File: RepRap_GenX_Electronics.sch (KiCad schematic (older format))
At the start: 105 parts, among them J1 AXIS_X, J10 END_Y, J11 END_Z, J12 END_E0, J13 END_E1, J14 HEAT_E1, J15 TEMP_BED, J16 TEMP_E0, J17 TEMP_E1, J18 E1, J19 Conn_ARM_JTAG_SWD_10, J2 AXIS_Y, J20 12V_0, J21 12V_1, J22 FAN_0, J23 FAN_1, J3 MOT_PWR, J3_1 AXIS_Z1, J3_2 AXIS_Z2, J4 E0, J5 HEAT_PWR, J6 HEAT_E0, J7 HEAT_BED, J8 USB_B_Micro, J9 END_X, Q1 IRLIZ44N, Q2 IRLIZ44N, Q3 IRLIZ44N, Q4 DMN2300U, Q5 DMN2300U, SW1 SW_Push, U1 STM32F412RGTx, U2 ADP2303ARDZ-5.0, U3 USBLC6-2SC6, U4 TPS62160DSG

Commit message: Added ZVD and 5V breakout for external supply
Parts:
- added J24: Conn_02x02_Counter_Clockwise, Connector_PinHeader_2.54mm:PinHeader_2x02_P2.54mm_Vertical, symbol Connector_Generic:Conn_02x02_Counter_Clockwise
- added Q6: DMMT5401-7(A), Package_SO:SC-74-6_1.5x2.9mm_P0.95mm, symbol Device:Q_DUAL_PNP_PNP_C1B1B2C2E2E1
- added Q7: DMG2305UX, Package_TO_SOT_SMD:SOT-23, symbol Transistor_FET:DMG2301L
- added R19, R4: 10K, Resistor_SMD:R_0603_1608Metric, symbol Device:R
- JP1: footprint Jumper:SolderJumper-2_P1.3mm_Open_TrianglePad1.0x1.5mm -> Connector_PinHeader_2.54mm:PinHeader_1x02_P2.54mm_Vertical
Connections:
- net +5V: now also Q6.6 (E1), Q7.3 (D); no longer C17.2, C5.1, J8.1 (VBUS), U3.5 (VBUS), U4.2 (VIN), U4.3 (EN)
- net GND: now also C13.1, J24.1 (Pin_1), J24.2 (Pin_2), R19.2, R4.2; no longer C13.2
- net at U1.30 (VCAP_1): now also C13.2; no longer C13.1
- new net: Q6.4 (C2), Q7.1 (G), R19.1
- new net: Q6.1 (C1), Q6.2 (B1), Q6.3 (B2), R4.1
- new net ZVD_5V: C17.2, C5.1, J24.3 (Pin_3), J24.4 (Pin_4), J8.1 (VBUS), Q6.5 (E2), Q7.2 (S), U3.5 (VBUS), U4.2 (VIN), U4.3 (EN)
- no-connect marks 13 -> 12
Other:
- note added: ""Ideal" Zero Volt Diode (ZVD)"
- moved on the sheet: C13, J19, J20, J21, XO1

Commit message: Added totem pole drivers for MOSFETs and split main schematic
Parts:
- removed A1, A2, A3, A4, A5: SilentStepStick_SPI, Module:Pololu_Breakout-16_15.2x20.3mm, symbol StepStick:SilentStepStick_SPI
- removed C19, C20, C21, C22, C23, C24, C25, C26, C27, C28: 100nF, Capacitor_SMD:C_0402_1005Metric, symbol Device:C
- removed D2, D3, D4: LED, LED_SMD:LED_0603_1608Metric, symbol Device:LED
- removed D5, D6, D7, D8, D9: D, Diode_SMD:D_SMA, symbol Device:D
- removed J1: AXIS_X, Connector_Molex:Molex_KK-254_AE-6410-04A_1x04_P2.54mm_Vertical, symbol Connector_Generic:Conn_01x04
- removed J10: END_Y, Connector_Molex:Molex_KK-254_AE-6410-03A_1x03_P2.54mm_Vertical, symbol Connector_Generic:Conn_01x03
- removed J11: END_Z, Connector_Molex:Molex_KK-254_AE-6410-03A_1x03_P2.54mm_Vertical, symbol Connector_Generic:Conn_01x03
- removed J12: END_E0, Connector_Molex:Molex_KK-254_AE-6410-03A_1x03_P2.54mm_Vertical, symbol Connector_Generic:Conn_01x03
- removed J13: END_E1, Connector_Molex:Molex_KK-254_AE-6410-03A_1x03_P2.54mm_Vertical, symbol Connector_Generic:Conn_01x03
- removed J14: HEAT_E1, Connector_Molex:Molex_KK-396_A-41791-0002_1x02_P3.96mm_Vertical, symbol Connector_Generic:Conn_01x02
- removed J15: TEMP_BED, Connector_Molex:Molex_KK-254_AE-6410-02A_1x02_P2.54mm_Vertical, symbol Connector_Generic:Conn_01x02
- removed J16: TEMP_E0, Connector_Molex:Molex_KK-254_AE-6410-02A_1x02_P2.54mm_Vertical, symbol Connector_Generic:Conn_01x02
- removed J17: TEMP_E1, Connector_Molex:Molex_KK-254_AE-6410-02A_1x02_P2.54mm_Vertical, symbol Connector_Generic:Conn_01x02
- removed J18: E1, Connector_Molex:Molex_KK-254_AE-6410-04A_1x04_P2.54mm_Vertical, symbol Connector_Generic:Conn_01x04
- removed J2: AXIS_Y, Connector_Molex:Molex_KK-254_AE-6410-04A_1x04_P2.54mm_Vertical, symbol Connector_Generic:Conn_01x04
- removed J22: FAN_0, Connector_Molex:Molex_KK-254_AE-6410-02A_1x02_P2.54mm_Vertical, symbol Connector_Generic:Conn_01x02
- removed J23: FAN_1, Connector_Molex:Molex_KK-254_AE-6410-02A_1x02_P2.54mm_Vertical, symbol Connector_Generic:Conn_01x02
- removed J3_1: AXIS_Z1, Connector_Molex:Molex_KK-254_AE-6410-04A_1x04_P2.54mm_Vertical, symbol Connector_Generic:Conn_01x04
- removed J3_2: AXIS_Z2, Connector_Molex:Molex_KK-254_AE-6410-04A_1x04_P2.54mm_Vertical, symbol Connector_Generic:Conn_01x04
- removed J4: E0, Connector_Molex:Molex_KK-254_AE-6410-04A_1x04_P2.54mm_Vertical, symbol Connector_Generic:Conn_01x04
- removed J6: HEAT_E0, Connector_Molex:Molex_KK-396_A-41791-0002_1x02_P3.96mm_Vertical, symbol Connector_Generic:Conn_01x02
- removed J7: HEAT_BED, Connector_Molex:Molex_KK-396_A-41791-0002_1x02_P3.96mm_Vertical, symbol Connector_Generic:Conn_01x02
- removed J9: END_X, Connector_Molex:Molex_KK-254_AE-6410-03A_1x03_P2.54mm_Vertical, symbol Connector_Generic:Conn_01x03
- removed Q1, Q2, Q3: IRLIZ44N, Package_TO_SOT_THT:TO-220F-3_Vertical, symbol Transistor_FET:IRLIZ44N
- removed Q4, Q5: DMN2300U, Package_TO_SOT_SMD:SOT-23, symbol Transistor_FET:BSS138
- removed R10, R17, R18, R8, R9: 1K, Resistor_SMD:R_0805_2012Metric, symbol Device:R
- removed R11, R12, R13: 4.7K, Resistor_SMD:R_0805_2012Metric, symbol Device:R
- removed R14, R15, R16: 2.2K, Resistor_SMD:R_0805_2012Metric, symbol Device:R
- added D10, D11: LG R971, LED_SMD:LED_0805_2012Metric_Castellated, symbol Device:LED
- added Q8: DMMT5401-7(A), Package_SO:SC-74-6_1.5x2.9mm_P0.95mm, symbol Device:Q_DUAL_PNP_PNP_C1B1B2C2E2E1
- added Q9: DMG2305UX, Package_TO_SOT_SMD:SOT-23, symbol Transistor_FET:DMG2301L
- added R20: 150 0.125W, Resistor_SMD:R_0603_1608Metric, symbol Device:R
- added R21: 56 0.125W, Resistor_SMD:R_0603_1608Metric, symbol Device:R
- added R22, R23: 10K, Resistor_SMD:R_0603_1608Metric, symbol Device:R
- C1: value 10uF -> 10uF 35V; Package Type (none) -> SMD 0603
- C10, C11, C12, C3, C30, C6, C9: value 100nF -> 100nF 6.3V; Package Type (none) -> SMD 0402
- C13, R1, R19, R2, R3, R4, R5, R6, R7: Package Type (none) -> SMD 0603
- C14: Package Type (none) -> SMD 0402
- C15, C17: value 1uF -> 1uF 6.3V; footprint Capacitor_SMD:C_0805_2012Metric -> Capacitor_SMD:C_0402_1005Metric; Package Type (none) -> SMD 0402
- C18: footprint Capacitor_SMD:C_0805_2012Metric -> Capacitor_SMD:C_0603_1608Metric; Package Type (none) -> SMD 0603
- C29: footprint Capacitor_SMD:C_0402_1005Metric -> Capacitor_SMD:C_0201_0603Metric; Package Type (none) -> SMD 0201
- C4: value 47uF -> 47uF 6.3V X5R; Mfr (none) -> Taiyo Yuden; Mfr PartNumber (none) -> JMK212BBJ476MG-T; Package Type (none) -> SMD 0805
- C5: value 10uF -> 10uF 6.3V; Package Type (none) -> SMD 0805
- D1: Mfr (none) -> ON Semiconductor; Mfr PartNumber (none) -> MBRS340T3G; Package Type (none) -> SMD D_SMC
- F1, F2, F3, G1, H1, H2, H3, H4, J20, J21, J24, J3, J5, JP1: Package Type (none) -> TH
- J19: Mfr (none) -> Harwin; Mfr PartNumber (none) -> M50-3600542; Package Type (none) -> SMT
- J8: Mfr (none) -> Molex; Mfr PartNumber (none) -> 47346-0001; Package Type (none) -> SMT
- L1, L2, L3, SW1, U2: Package Type (none) -> SMT
- Q6: Mfr (none) -> DIODES; Mfr PartNumber (none) -> DMMT5401; Package Type (none) -> SMT
- Q7: Mfr (none) -> DIODES; Mfr PartNumber (none) -> DMG2305UX; Package Type (none) -> SMT
- U1: Mfr (none) -> ST Microelectronics; Mfr PartNumber (none) -> STM32F412RGT6; Package Type (none) -> SMT
- U3: Mfr (none) -> ST Microelectronics; Mfr PartNumber (none) -> USBLC6-2SC6; Package Type (none) -> SMT
- U4: Mfr (none) -> TI; Mfr PartNumber (none) -> TPS62160DSG; Package Type (none) -> SMT
- XO1: Mfr (none) -> Epson; Mfr PartNumber (none) -> Q33519E40001912; Package Type (none) -> SMT
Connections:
- net +5V: now also Q8.5 (E2), Q9.2 (S), R20.1
- net CS_E0: now also U1.37 (PC6); no longer U1.35 (PB14)
- net CS_E1: now also U1.41 (PA8); no longer U1.39 (PC8)
- net DIR_E0: now also U1.39 (PC8); no longer U1.37 (PC6)
- net DIR_E1: now also U1.43 (PA10); no longer U1.41 (PA8)
- net EN_E0: now also U1.36 (PB15); no longer U1.34 (PB13)
- net EN_E1: now also U1.40 (PC9); no longer U1.38 (PC7)
- net GND: now also D10.1 (K), D11.1 (K), R22.2, R23.2
- net PWM_FAN0: now also U1.35 (PB14); no longer U1.42 (PA9)
- net PWM_FAN1: now also U1.34 (PB13); no longer U1.43 (PA10)
- net STEP_E0: now also U1.38 (PC7); no longer U1.36 (PB15)
- net STEP_E1: now also U1.42 (PA9); no longer U1.40 (PC9)
- net VDD: now also R21.1
- net ZVD_5V: no longer C17.2, J8.1 (VBUS), U3.5 (VBUS)
- new net: D10.2 (A), R20.2
- new net: D11.2 (A), R21.2
- new net: Q8.4 (C2), Q9.1 (G), R23.1
- new net: Q8.1 (C1), Q8.2 (B1), Q8.3 (B2), R22.1
- new net USB_5V: C17.2, J8.1 (VBUS), Q8.6 (E1), Q9.3 (D), U3.5 (VBUS)
- no-connect marks 12 -> 7
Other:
- note added: ""Ideal" Diode (ZVD)"
- note removed: ""Ideal" Zero Volt Diode (ZVD)"
- moved on the sheet: C17, H1, H2, H3, H4, J20, J21, J24, J8, L1, Q6A, Q6B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

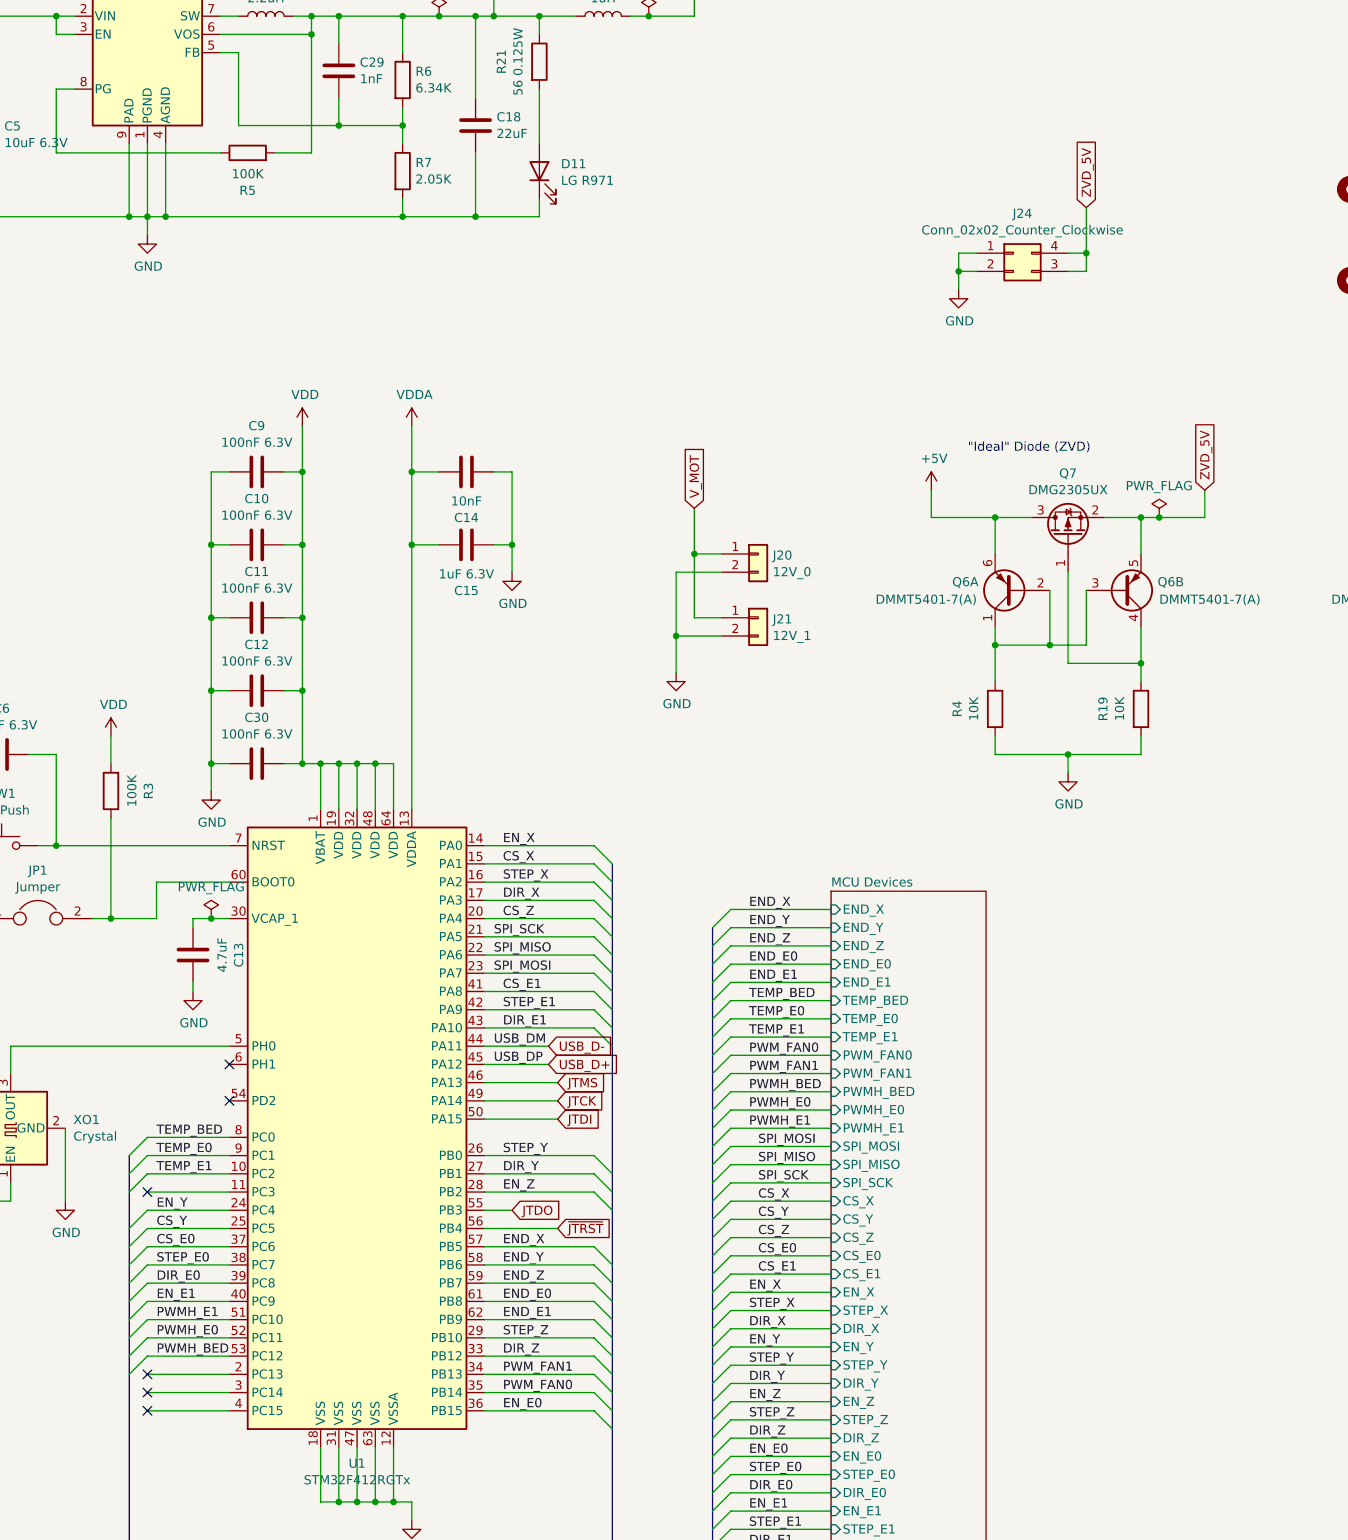
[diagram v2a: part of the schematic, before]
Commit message: Added I2C and 3.3v breakout for expansion port
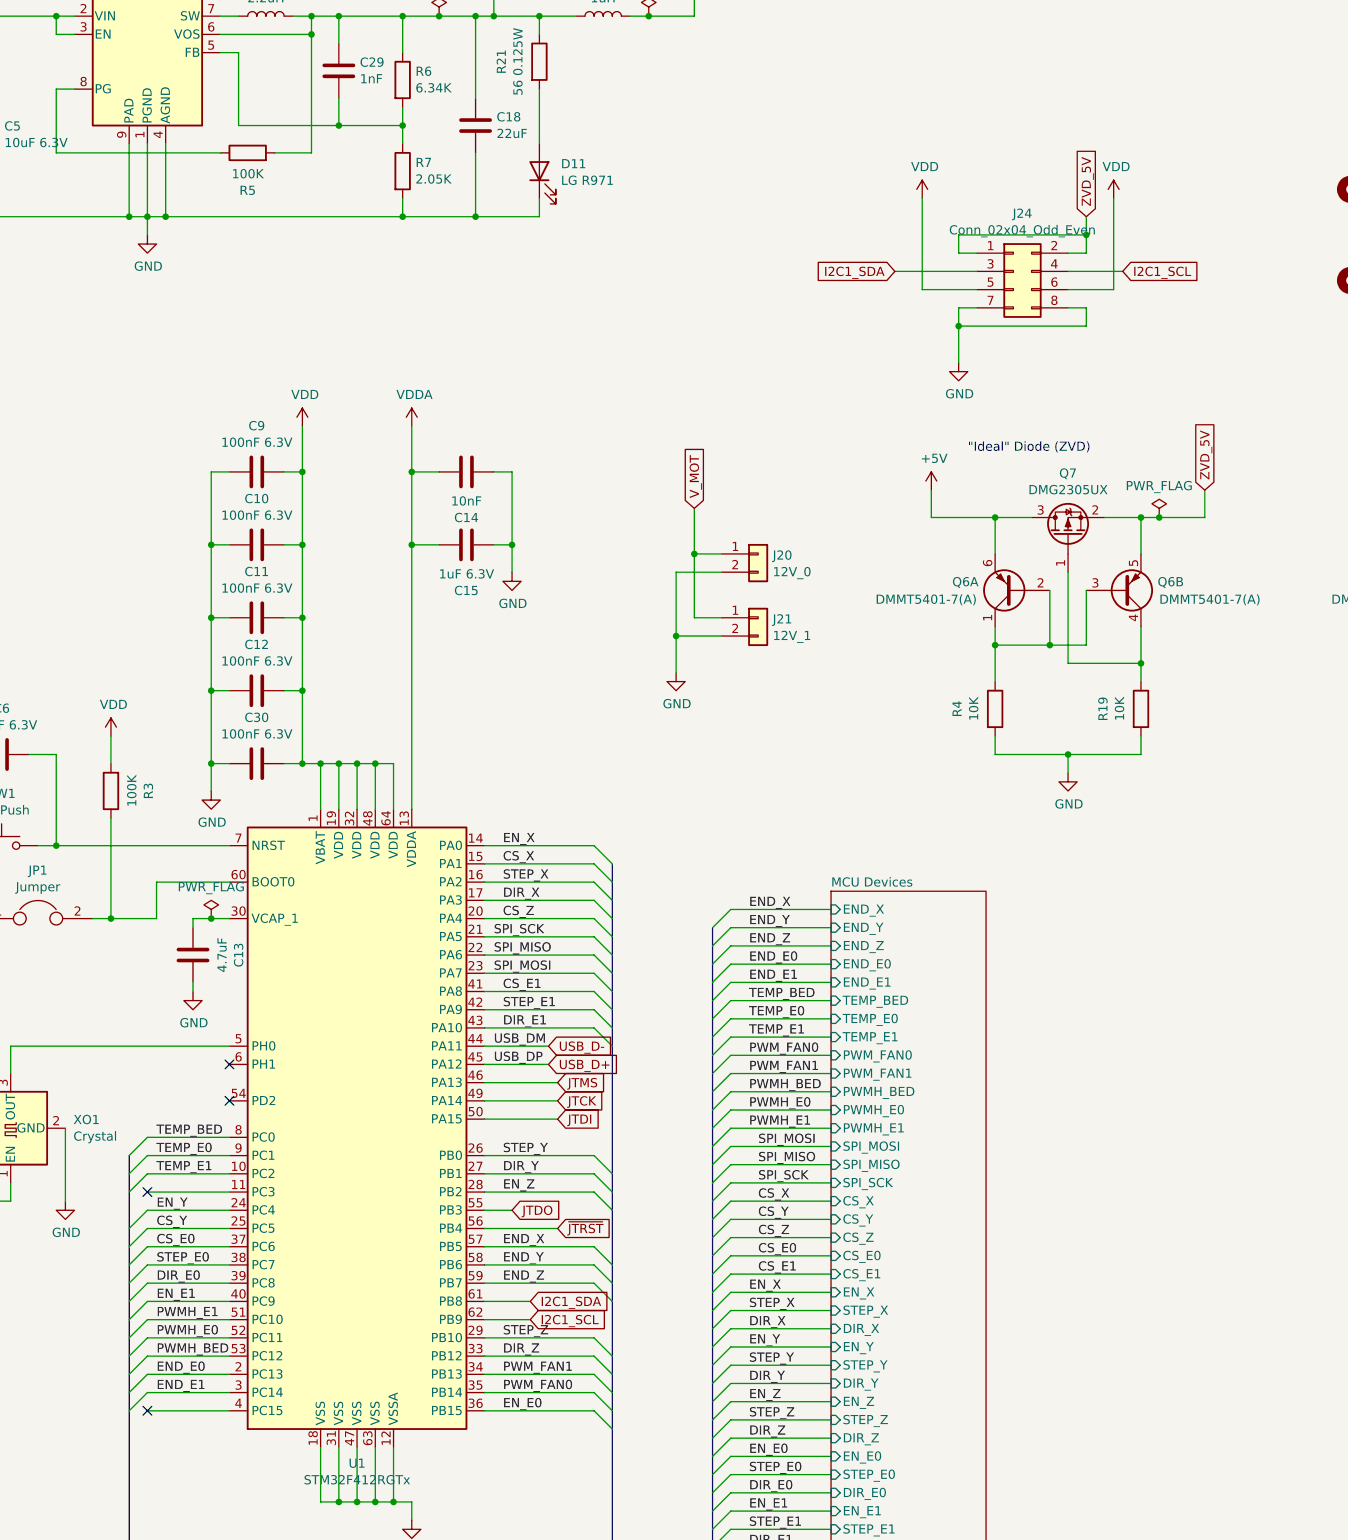
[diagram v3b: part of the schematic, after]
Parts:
- removed J24: Conn_02x02_Counter_Clockwise, Connector_PinHeader_2.54mm:PinHeader_2x02_P2.54mm_Vertical, symbol Connector_Generic:Conn_02x02_Counter_Clockwise
- added J24: Conn_02x04_Odd_Even, Connector_PinHeader_2.54mm:PinHeader_2x04_P2.54mm_Vertical, symbol Connector_Generic:Conn_02x04_Odd_Even
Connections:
- net END_E0: now also U1.2 (PC13); no longer U1.61 (PB8)
- net END_E1: now also U1.3 (PC14); no longer U1.62 (PB9)
- net GND: now also J24.7 (Pin_7), J24.8 (Pin_8)
- net VDD: now also J24.5 (Pin_5), J24.6 (Pin_6)
- net ZVD_5V: now also J24.1 (Pin_1), J24.2 (Pin_2)
- new net I2C1_SCL: J24.4 (Pin_4), U1.62 (PB9)
- new net I2C1_SDA: J24.3 (Pin_3), U1.61 (PB8)
- no-connect marks 7 -> 5
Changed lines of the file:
@@
 	8400 8650 8500 8750
-Entry Wire Line
-	8400 8550 8500 8650
-Entry Wire Line
-	8400 8450 8500 8550
 Entry Wire Line
 	8400 8350 8500 8450
@@
 Text Label 7900 8150 0    50   ~ 0
 END_X
-Text Label 7900 8450 0    50   ~ 0
+Text Label 6000 8850 0    50   ~ 0
 END_E0
-Text Label 7900 8550 0    50   ~ 0
+Text Label 6000 8950 0    50   ~ 0
 END_E1
 Wire Wire Line
@@
 	1    0    0    -1
 $EndComp
-Wire Wire Line
-	7800 8550 8400 8550
-Wire Wire Line
-	7800 8450 8400 8450
 Wire Wire Line
 	7800 8350 8400 8350
@@
 Entry Wire Line
 	5950 8750 5850 8850
-NoConn ~ 5950 8850
 Wire Wire Line
 	7800 7350 8200 7350
@@
 	1    0    0    -1
 $EndComp
-NoConn ~ 5950 8950
 Wire Wire Line
 	6400 8950 5950 8950
@@
 	4150 1700 4350 1700
 $Comp
-L Connector_Generic:Conn_02x02_Counter_Clockwise J24
-U 1 1 60E81E8D
-P 10700 2700
-F 0 "J24" H 10750 2917 50  0000 C CNN
-F 1 "Conn_02x02_Counter_Clockwise" H 10750 2826 50  0000 C CNN
-F 2 "Connector_PinHeader_2.54mm:PinHeader_2x02_P2.54mm_Vertical" H 10700 2700 50  0001 C CNN
-F 3 "~" H 10700 2700 50  0001 C CNN
-F 4 "TH" H 10700 2700 50  0001 C CNN "Package Type"
-	1    10700 2700
-	1    0    0    -1
-$EndComp
-Wire Wire Line
-	10500 2700 10400 2700
-Wire Wire Line
-	10400 2700 10400 2800
-Wire Wire Line
-	10400 2800 10500 2800
-Wire Wire Line
-	11100 2800 11100 2700
-Wire Wire Line
-	11100 2700 11000 2700
-Wire Wire Line
-	11000 2800 11100 2800
-$Comp
 L power:GND #PWR07
 U 1 1 60FD29A0
-P 10400 2900
-F 0 "#PWR07" H 10400 2650 50  0001 C CNN
-F 1 "GND" H 10405 2727 50  0000 C CNN
-F 2 "" H 10400 2900 50  0001 C CNN
-F 3 "" H 10400 2900 50  0001 C CNN
-	1    10400 2900
-	1    0    0    -1
-$EndComp
-Wire Wire Line
-	10400 2900 10400 2800
-Connection ~ 10400 2800
-Text GLabel 11100 2450 1    50   Input ~ 0
+P 10400 3300
+F 0 "#PWR07" H 10400 3050 50  0001 C CNN
+F 1 "GND" H 10405 3127 50  0000 C CNN
+F 2 "" H 10400 3300 50  0001 C CNN
+F 3 "" H 10400 3300 50  0001 C CNN
+	1    10400 3300
+	1    0    0    -1
+$EndComp
+Text GLabel 11100 2500 1    50   Input ~ 0
 ZVD_5V
-Wire Wire Line
-	11100 2450 11100 2700
-Connection ~ 11100 2700
 NoConn ~ 6400 7350
 $Comp
@@
 Text Notes 12600 9750 0    50   ~ 0
 Copyright NerdSmith.co.uk 2020.\n\nThis source describes Open Hardware and is licensed under the CERN-OHL-Pv2\n\nYou may redistribute and modify this documentation and make products\nusing it under the terms of the CERN-OHL-P v2 (https:/cern.ch/cern-ohl).\nThis documentation is distributed WITHOUT ANY EXPRESS OR IMPLIED\nWARRANTY, INCLUDING OF MERCHANTABILITY, SATISFACTORY QUALITY\nAND FITNESS FOR A PARTICULAR PURPOSE. Please see the CERN-OHL-P v2\nfor applicable conditions
+Entry Wire Line
+	5950 8850 5850 8950
+Entry Wire Line
+	5950 8950 5850 9050
+Text GLabel 8050 8450 2    50   Input ~ 0
+I2C1_SDA
+Text GLabel 8050 8550 2    50   Input ~ 0
+I2C1_SCL
+Wire Wire Line
+	7800 8450 8050 8450
+Wire Wire Line
+	7800 8550 8050 8550
+Text GLabel 10050 2800 0    50   Input ~ 0
+I2C1_SDA
+Text GLabel 11300 2800 2    50   Input ~ 0
+I2C1_SCL
+Wire Wire Line
+	11300 2800 11000 2800
+Wire Wire Line
+	10500 2800 10050 2800
+Wire Wire Line
+	11000 3000 11100 3000
+Wire Wire Line
+	11100 3000 11100 3100
+Wire Wire Line
+	11100 3100 10400 3100
+Wire Wire Line
+	10400 3100 10400 3000
+Wire Wire Line
+	10400 3000 10500 3000
+Wire Wire Line
+	10400 3100 10400 3300
+Connection ~ 10400 3100
+Wire Wire Line
+	10500 2700 10400 2700
+Wire Wire Line
+	10400 2700 10400 2600
+Wire Wire Line
+	10400 2600 11100 2600
+Wire Wire Line
+	11100 2600 11100 2700
+Wire Wire Line
+	11100 2700 11000 2700
+Wire Wire Line
+	11100 2600 11100 2500
+Connection ~ 11100 2600
+$Comp
+L Connector_Generic:Conn_02x04_Odd_Even J24
+U 1 1 605418FF
+P 10700 2800
+F 0 "J24" H 10750 3117 50  0000 C CNN
+F 1 "Conn_02x04_Odd_Even" H 10750 3026 50  0000 C CNN
+F 2 "Connector_PinHeader_2.54mm:PinHeader_2x04_P2.54mm_Vertical" H 10700 2800 50  0001 C CNN
+F 3 "~" H 10700 2800 50  0001 C CNN
+	1    10700 2800
+	1    0    0    -1
+$EndComp
+Wire Wire Line
+	10500 2900 10200 2900
+Wire Wire Line
+	10200 2900 10200 2400
+Wire Wire Line
+	11000 2900 11250 2900
+Wire Wire Line
+	11250 2900 11250 2400
 Wire Bus Line
 	5850 7650 5850 10350
@@
 Wire Bus Line
 	9050 6400 9050 10350
+$Comp
+L power:VDD #PWR0118
+U 1 1 6063A334
+P 10200 2400
+F 0 "#PWR0118" H 10200 2250 50  0001 C CNN
+F 1 "VDD" H 10215 2573 50  0000 C CNN
+F 2 "" H 10200 2400 50  0001 C CNN
+F 3 "" H 10200 2400 50  0001 C CNN
+	1    10200 2400
+	1    0    0    -1
+$EndComp
+$Comp
+L power:VDD #PWR0119
+U 1 1 6063ACAF
+P 11250 2400
+F 0 "#PWR0119" H 11250 2250 50  0001 C CNN
+F 1 "VDD" H 11265 2573 50  0000 C CNN
+F 2 "" H 11250 2400 50  0001 C CNN
+F 3 "" H 11250 2400 50  0001 C CNN
+	1    11250 2400
+	1    0    0    -1
+$EndComp
 $EndSCHEMATC
